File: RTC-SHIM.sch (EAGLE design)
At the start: 5 parts, among them IC1 DS3231/SO

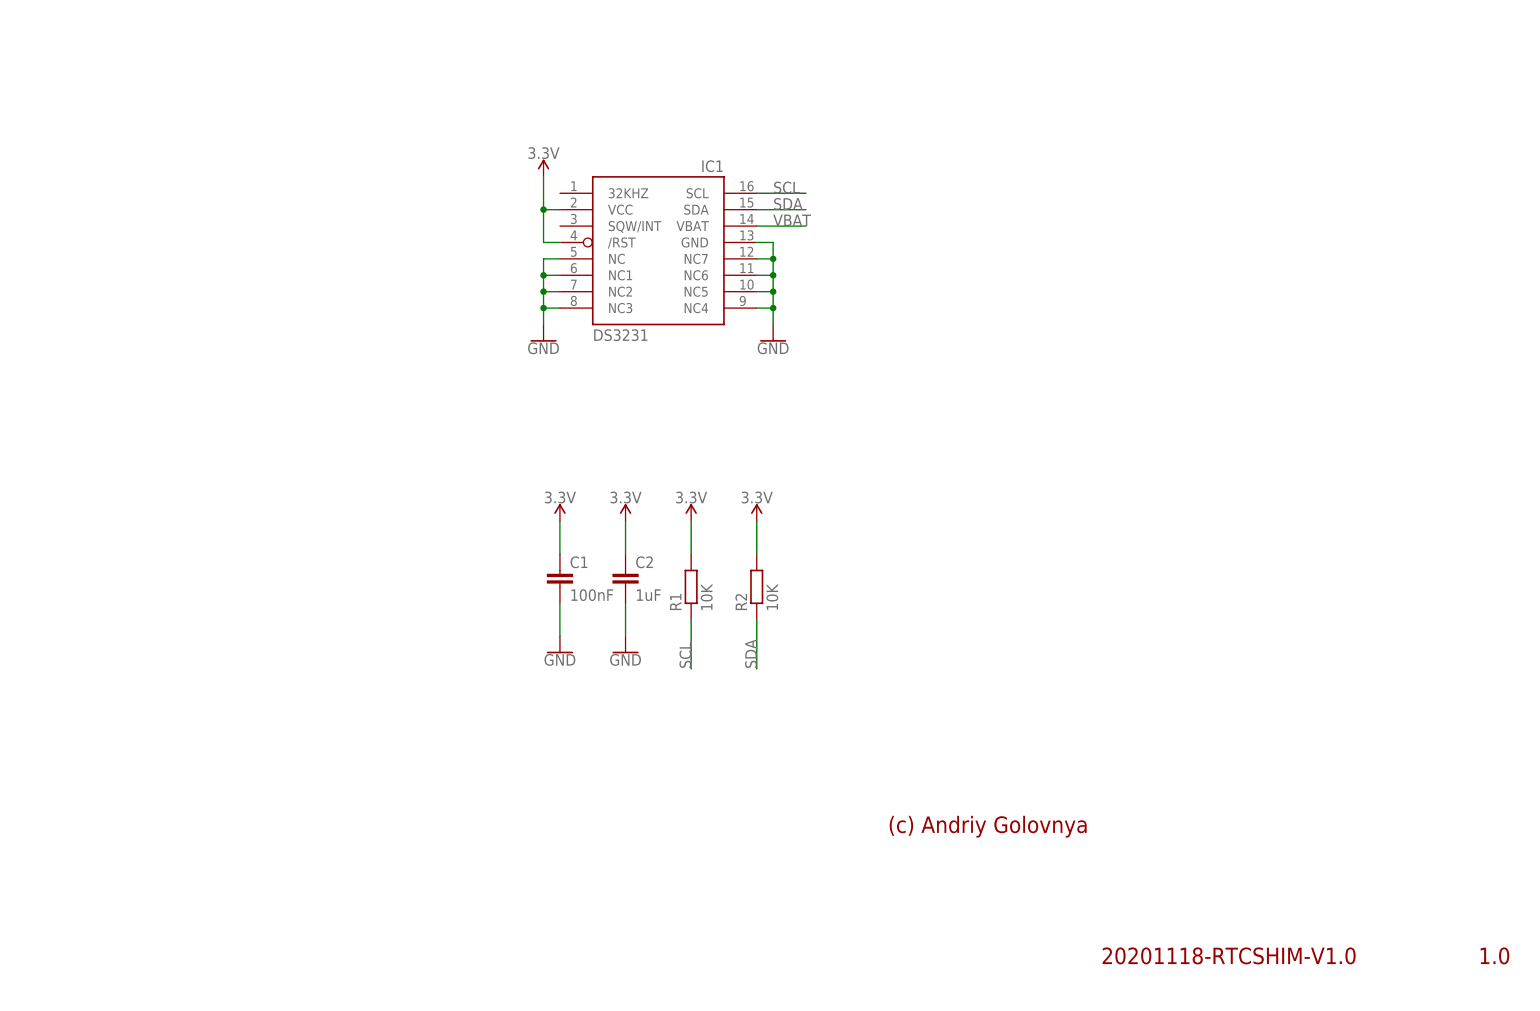
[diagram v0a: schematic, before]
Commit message: Add 40 pin connectors and solder joins fro I2C bus selection. Add basic board layout.
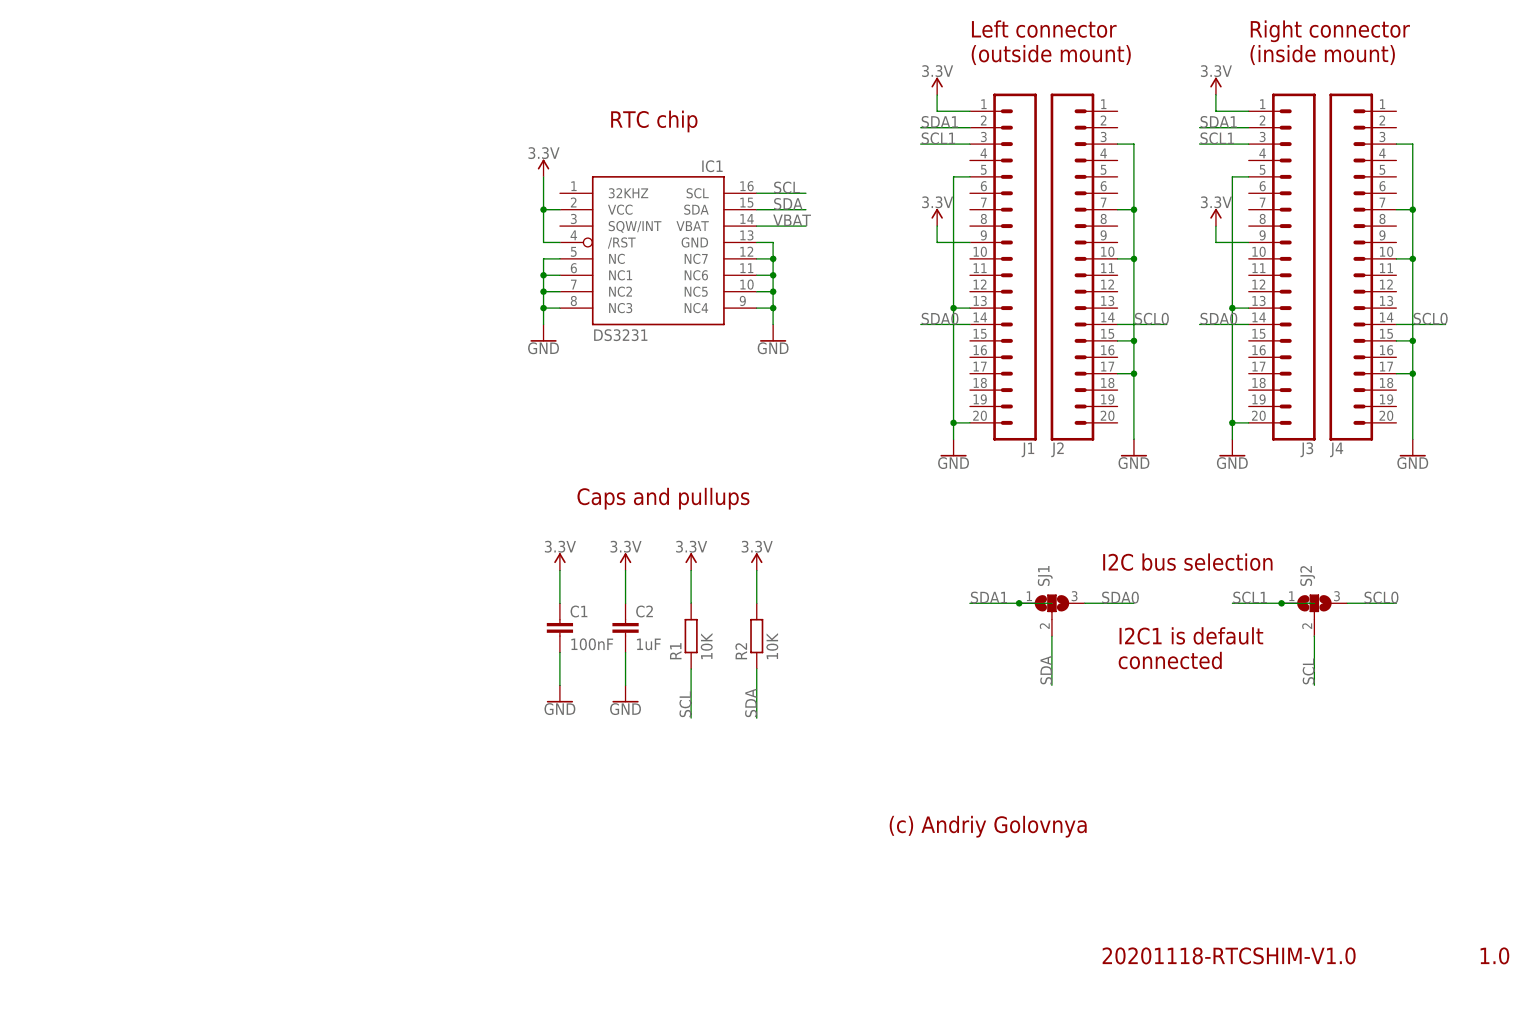
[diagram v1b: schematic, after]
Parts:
- added J1, J2, J3, J4: (no value), SparkFun-Connectors:CONN_20LOCK_NOSILK
- added SJ1, SJ2: (no value), _my_jumpers:SJ2
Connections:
- new net SCL0: J2.14, J4.14, SJ2.3
- new net SCL1: J1.3, J3.3, SJ2.1
- new net SDA0: J1.14, J3.14, SJ1.3
- new net SDA1: J1.2, J3.2, SJ1.1
- net 3.3V: now also J1.1, J1.9, J3.1, J3.9
- net GND: now also J1.13, J1.20, J1.5, J2.10, J2.15, J2.17, J2.3, J2.7, J3.13, J3.20, J3.5, J4.10, J4.15, J4.17, J4.3, J4.7
- net SCL: now also SJ2.2
- net SDA: now also SJ1.2
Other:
- note added: "Caps and pullups"
- note added: "I2C bus selection"
- note added: "I2C1 is default connected"
- note added: "Left connector (outside mount)"
- note added: "RTC chip"
- note added: "Right connector (inside mount)"
- moved on the sheet: C1, C2, R1, R2

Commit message: Added Battery holder and some logos and texts.
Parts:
- added BAT1: CR1220-2, CR1220-2:CR1220-2
- added LOGO1: MFDECLOGO_SQ_8MM, _my_logos:MFDECLOGO_SQ_8MM
- added LOGO2: MFDECLOGO_L_20MM, _my_logos:MFDECLOGO_L_20MM
- added LOGO3: RSNURL_QR_10MM, _my_logos:RSNURL_QR_10MM
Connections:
- net GND: now also BAT1.BAT-
- net VBAT: now also BAT1.BAT+
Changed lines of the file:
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@@
 <part name="SJ1" library="_my_jumpers" deviceset="SJ2" device=""/>
 <part name="SJ2" library="_my_jumpers" deviceset="SJ2" device=""/>
+<part name="BAT1" library="CR1220-2" deviceset="CR1220-2" device=""/>
+<part name="GND9" library="SparkFun-PowerSymbols" library_urn="urn:adsk.eagle:library:530" deviceset="GND" device=""/>
+<part name="LOGO1" library="_my_logos" deviceset="MFDECLOGO" device="_SQ_8MM" value="MFDECLOGO_SQ_8MM"/>
+<part name="LOGO2" library="_my_logos" deviceset="MFDECLOGO" device="_L_20MM" value="MFDECLOGO_L_20MM"/>
+<part name="LOGO3" library="_my_logos" deviceset="RSNURL" device="_QR_10MM"/>
 </parts>
 <sheets>
@@
 <attribute name="VALUE" x="233.045" y="66.04" size="1.778" layer="96" rot="R90"/>
 </instance>
+<instance part="BAT1" gate="G$1" x="48.26" y="119.38" smashed="yes">
+<attribute name="NAME" x="45.72" y="124.46" size="1.27" layer="96"/>
+<attribute name="VALUE" x="45.72" y="114.3" size="1.27" layer="96"/>
+</instance>
+<instance part="GND9" gate="1" x="58.42" y="116.84" smashed="yes">
+<attribute name="VALUE" x="58.42" y="116.586" size="1.778" layer="96" align="top-center"/>
+</instance>
+<instance part="LOGO1" gate="G$1" x="236.22" y="25.4" smashed="yes"/>
+<instance part="LOGO2" gate="G$1" x="208.28" y="25.4" smashed="yes"/>
+<instance part="LOGO3" gate="G$1" x="139.7" y="2.54" smashed="yes"/>
 </instances>
 <busses>
@@
 <wire x1="144.78" y1="121.92" x2="152.4" y2="121.92" width="0.1524" layer="91"/>
 <label x="147.32" y="121.92" size="1.778" layer="95"/>
+</segment>
+<segment>
+<pinref part="BAT1" gate="G$1" pin="BAT+"/>
+<wire x1="45.72" y1="119.38" x2="38.1" y2="119.38" width="0.1524" layer="91"/>
+<label x="35.56" y="119.38" size="1.778" layer="95"/>
 </segment>
 </net>
@@
 <junction x="246.38" y="99.06"/>
 </segment>
-</net>
+<segment>
+<pinref part="BAT1" gate="G$1" pin="BAT-"/>
+<wire x1="53.34" y1="119.38" x2="58.42" y2="119.38" width="0.1524" layer="91"/>
+<pinref part="GND9" gate="1" pin="GND"/>
+</segment>
+</net>

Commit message: Moved stuff around a little bit.
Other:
- note added: "Battery holder"
- moved on the sheet: C1, C2, IC1, J1, J2, J3, J4, R1, R2, SJ1, SJ2

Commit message: Trace the board. Add CAM files.
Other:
- note added: "I2C1 is connected by default"
- note removed: "I2C1 is default connected"
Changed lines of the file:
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@@
 (inside mount)</text>
 <text x="208.28" y="81.28" size="2.54" layer="94">I2C bus selection</text>
-<text x="210.82" y="63.5" size="2.54" layer="94">I2C1 is default
-connected</text>
+<text x="208.28" y="60.96" size="2.54" layer="94">I2C1 is connected
+by default</text>
 <text x="210.82" y="127" size="2.54" layer="94">Battery holder</text>
 </plain>
@@
 <instance part="J1" gate="G$1" x="114.3" y="121.92" smashed="yes" rot="R180">
 <attribute name="VALUE" x="114.3" y="121.666" size="1.778" layer="96" font="vector" rot="R180"/>
-<attribute name="NAME" x="114.3" y="65.532" size="1.778" layer="95" font="vector" rot="R180"/>
+<attribute name="NAME" x="114.3" y="65.532" size="1.778" layer="95" rot="R180"/>
 </instance>
 <instance part="J2" gate="G$1" x="116.84" y="121.92" smashed="yes" rot="MR180">
 <attribute name="VALUE" x="116.84" y="121.666" size="1.778" layer="96" font="vector" rot="MR180"/>
-<attribute name="NAME" x="116.84" y="65.532" size="1.778" layer="95" font="vector" rot="MR180"/>
+<attribute name="NAME" x="116.84" y="65.532" size="1.778" layer="95" rot="MR180"/>
 </instance>
 <instance part="SUPPLY6" gate="G$1" x="99.06" y="119.38" smashed="yes">
@@
 <instance part="J3" gate="G$1" x="157.48" y="121.92" smashed="yes" rot="R180">
 <attribute name="VALUE" x="157.48" y="121.666" size="1.778" layer="96" font="vector" rot="R180"/>
-<attribute name="NAME" x="157.48" y="65.532" size="1.778" layer="95" font="vector" rot="R180"/>
+<attribute name="NAME" x="157.48" y="65.532" size="1.778" layer="95" rot="R180"/>
 </instance>
 <instance part="J4" gate="G$1" x="160.02" y="121.92" smashed="yes" rot="MR180">
 <attribute name="VALUE" x="160.02" y="121.666" size="1.778" layer="96" font="vector" rot="MR180"/>
-<attribute name="NAME" x="160.02" y="65.532" size="1.778" layer="95" font="vector" rot="MR180"/>
+<attribute name="NAME" x="160.02" y="65.532" size="1.778" layer="95" rot="MR180"/>
 </instance>
 <instance part="SUPPLY8" gate="G$1" x="142.24" y="119.38" smashed="yes">
